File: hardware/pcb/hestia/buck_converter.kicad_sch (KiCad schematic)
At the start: 21 parts

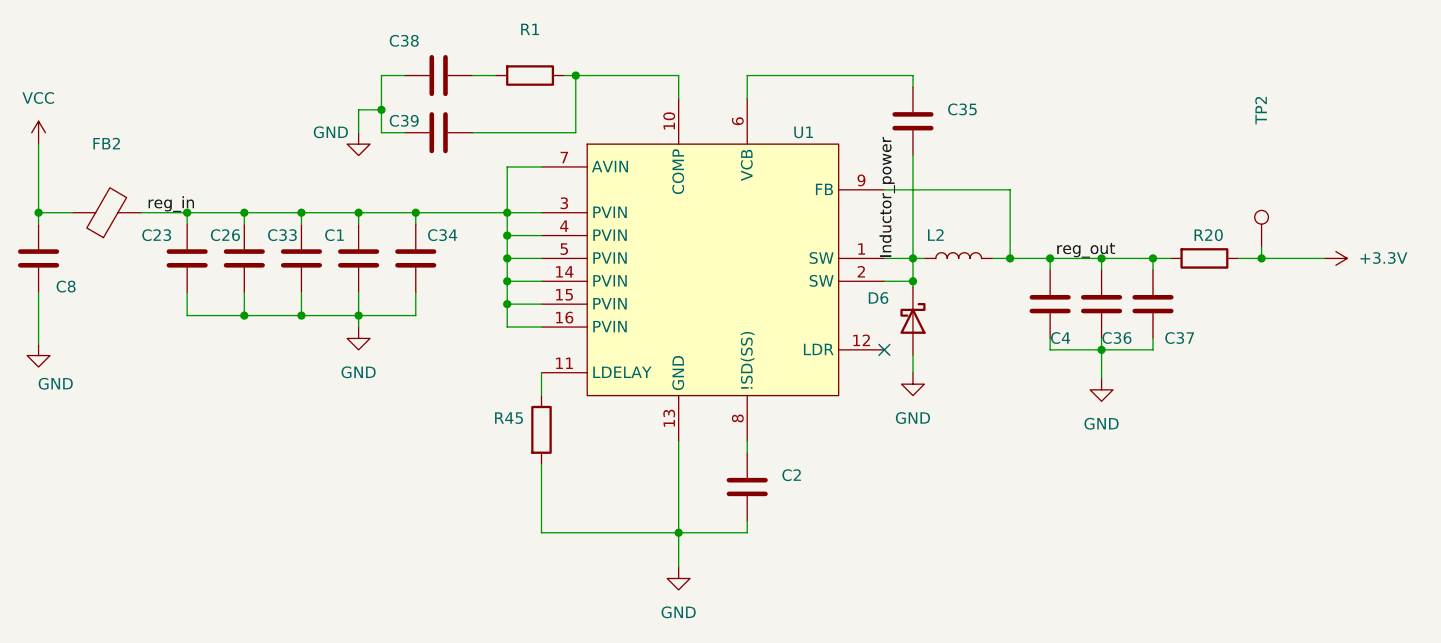
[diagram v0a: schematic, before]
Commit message: Fix some ERC violations
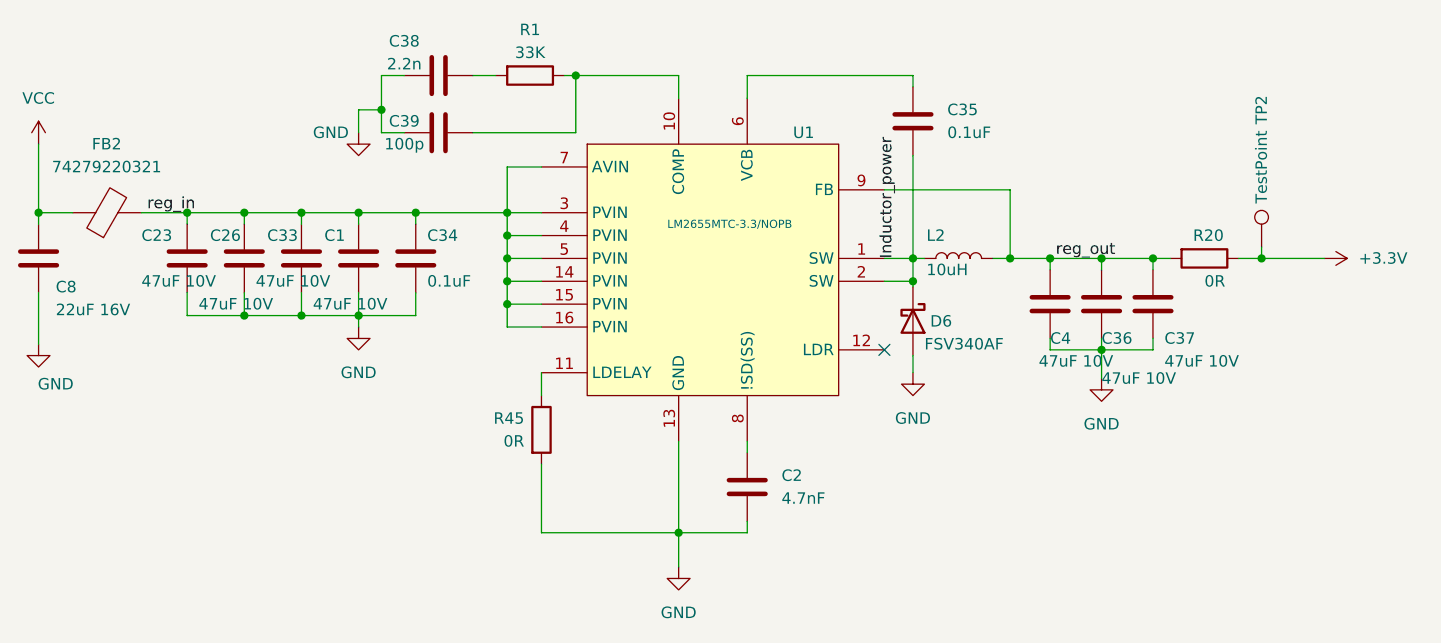
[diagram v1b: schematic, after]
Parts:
- C1, C23, C26, C33, C36, C37, C4: value (none) -> 47uF 10V; footprint (none) -> Capacitor_SMD:C_0805_2012Metric_Pad1.18x1.45mm_HandSolder
- C2: value (none) -> 4.7nF; footprint (none) -> Capacitor_SMD:C_0603_1608Metric_Pad1.08x0.95mm_HandSolder
- C34, C35: value (none) -> 0.1uF; footprint (none) -> Capacitor_SMD:C_0603_1608Metric_Pad1.08x0.95mm_HandSolder
- C38: value (none) -> 2.2n; footprint (none) -> Capacitor_SMD:C_0603_1608Metric_Pad1.08x0.95mm_HandSolder
- C39: value (none) -> 100p; footprint (none) -> Capacitor_SMD:C_0603_1608Metric_Pad1.08x0.95mm_HandSolder
- C8: value (none) -> 22uF 16V; footprint (none) -> Capacitor_SMD:C_1206_3216Metric
- D6: value (none) -> FSV340AF; footprint (none) -> Hestia:DO-214AD (SMAF)
- FB2: value (none) -> 74279220321; footprint (none) -> Resistor_SMD:R_0805_2012Metric_Pad1.20x1.40mm_HandSolder
- L2: value (none) -> 10uH; footprint (none) -> Inductor_SMD:L_Coilcraft_LPS5030
- R1: value (none) -> 33K; footprint (none) -> Resistor_SMD:R_0603_1608Metric_Pad0.98x0.95mm_HandSolder
- R20: value (none) -> 0R; footprint (none) -> Resistor_SMD:R_1210_3225Metric_Pad1.30x2.65mm_HandSolder
- R45: value (none) -> 0R; footprint (none) -> Resistor_SMD:R_0603_1608Metric_Pad0.98x0.95mm_HandSolder
- TP2: value (none) -> TestPoint; footprint (none) -> TestPoint:TestPoint_Pad_2.0x2.0mm
- U1: value (none) -> LM2655MTC-3.3/NOPB; footprint (none) -> Package_SO:TSSOP-16_4.4x5mm_P0.65mm
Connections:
- net +3V3 renamed +3.3V

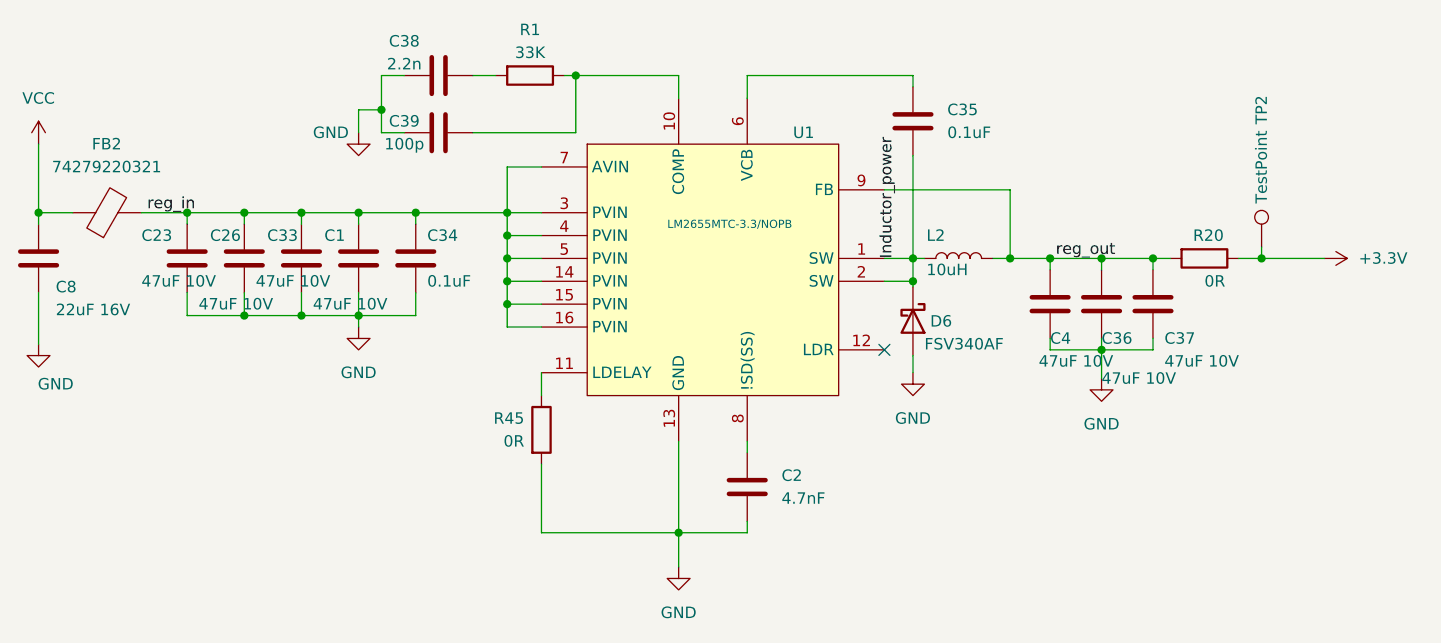
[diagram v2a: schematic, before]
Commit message: changed all 10K to 0.5% to be same component. changed led part numbers back to 0805. - my mistake. i had thought the footprints had changed to 0603. filled in other missing digikey part numbers. added manufacturer names and manufacturer part numbers. finished adding SMD/TH entry for component types. Excluded R4/R5 DNP part numbers from BOM
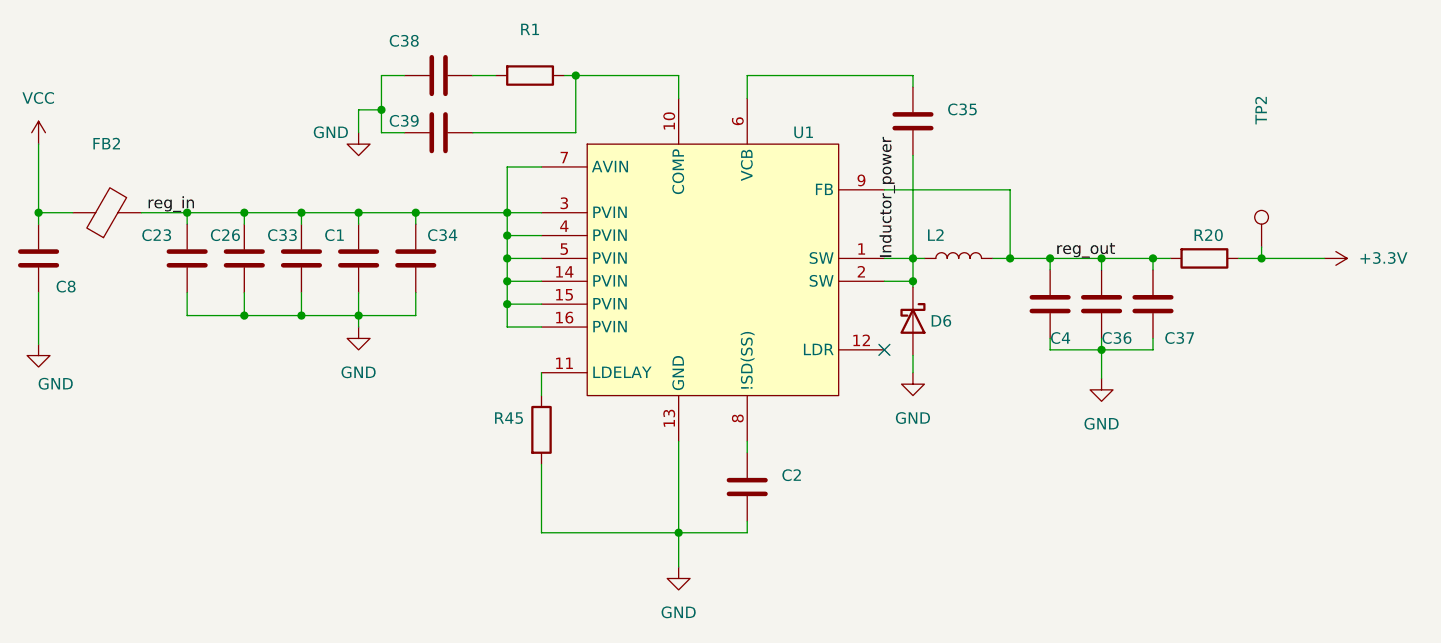
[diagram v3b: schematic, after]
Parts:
- C1, C23, C26, C33, C36, C37, C4: value 47uF 10V -> (none); footprint Capacitor_SMD:C_0805_2012Metric_Pad1.18x1.45mm_HandSolder -> (none); Manufacturer (none) -> Taiyo Yuden; Mfr PN (none) -> LMK212BBJ476MG-T
- C2: value 4.7nF -> (none); footprint Capacitor_SMD:C_0603_1608Metric_Pad1.08x0.95mm_HandSolder -> (none); Manufacturer (none) -> Samsung Electro-Mechanics; Mfr PN (none) -> CL10B472KB8WPNC
- C34, C35: value 0.1uF -> (none); footprint Capacitor_SMD:C_0603_1608Metric_Pad1.08x0.95mm_HandSolder -> (none); Manufacturer (none) -> Samsung Electro-Mechanics; Mfr PN (none) -> CL10B104KB8WPND
- C38: value 2.2n -> (none); footprint Capacitor_SMD:C_0603_1608Metric_Pad1.08x0.95mm_HandSolder -> (none); Manufacturer (none) -> KEMET; Mfr PN (none) -> C0603C222K5RACAUTO
- C39: value 100p -> (none); footprint Capacitor_SMD:C_0603_1608Metric_Pad1.08x0.95mm_HandSolder -> (none); Manufacturer (none) -> KYOCERA AVX; Mfr PN (none) -> 06035A100FAT2A
- C8: value 22uF 16V -> (none); footprint Capacitor_SMD:C_1206_3216Metric -> (none); Manufacturer (none) -> Samsung Electro-Mechanics; Mfr PN (none) -> CL31A226MOCLNNC; Type (none) -> SMD
- D6: value FSV340AF -> (none); footprint Hestia:DO-214AD (SMAF) -> (none); Manufacturer (none) -> onsemi; Mfr PN (none) -> FSV340AF
- FB2: value 74279220321 -> (none); footprint Resistor_SMD:R_0805_2012Metric_Pad1.20x1.40mm_HandSolder -> (none); Manufacturer (none) -> Würth Elektronik; Mfr PN (none) -> 74279220321
- L2: value 10uH -> (none); footprint Inductor_SMD:L_Coilcraft_LPS5030 -> (none); Manufacturer (none) -> Bourns Inc.; Mfr PN (none) -> SRP5030C-100M
- R1: value 33K -> (none); footprint Resistor_SMD:R_0603_1608Metric_Pad0.98x0.95mm_HandSolder -> (none); Digikey Part ERJ-PA3F3302V -> P33KBYCT-ND; Manufacturer (none) -> Panasonic Electronic Components; Mfr PN (none) -> ERJ-PA3F3302V
- R20: value 0R -> (none); footprint Resistor_SMD:R_1210_3225Metric_Pad1.30x2.65mm_HandSolder -> (none); Digikey Part (none) -> YAG3375CT-ND; Manufacturer (none) -> YAGEO; Mfr PN (none) -> RC1210JR-070RL
- R45: value 0R -> (none); footprint Resistor_SMD:R_0603_1608Metric_Pad0.98x0.95mm_HandSolder -> (none); Digikey Part (none) -> RMCF0603ZT0R00CT-ND; Manufacturer (none) -> Stackpole Electronics Inc; Mfr PN (none) -> RMCF0603ZT0R00
- TP2: value TestPoint -> (none); footprint TestPoint:TestPoint_Pad_2.0x2.0mm -> (none)
- U1: value LM2655MTC-3.3/NOPB -> (none); footprint Package_SO:TSSOP-16_4.4x5mm_P0.65mm -> (none); Manufacturer TI -> Texas Instruments; Mfr PN (none) -> LM2655MTC-3.3/NOPB

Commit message: c39 digikey and mfr part numbers changed to a 100pf part number. It had previously erroneously been given a 10pf part number
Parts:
- C39: Digikey Part 478-10285-1-ND -> 720-1649-1-ND; Manufacturer KYOCERA AVX -> Vishay Vitramon; Mfr PN 06035A100FAT2A -> VJ0603A101FXACW1BC
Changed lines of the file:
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@@
       (effects (font (size 1.27 1.27)) hide)
     )
-    (property "Digikey Part" "478-10285-1-ND" (id 5) (at 121.285 76.835 0)
+    (property "Digikey Part" "720-1649-1-ND" (id 5) (at 121.285 76.835 0)
       (effects (font (size 1.27 1.27)) hide)
     )
-    (property "Manufacturer" "KYOCERA AVX" (id 6) (at 121.285 76.835 0)
+    (property "Manufacturer" "Vishay Vitramon" (id 6) (at 121.285 76.835 0)
       (effects (font (size 1.27 1.27)) hide)
     )
-    (property "Mfr PN" "06035A100FAT2A" (id 7) (at 121.285 76.835 0)
+    (property "Mfr PN" "VJ0603A101FXACW1BC" (id 7) (at 121.285 76.835 0)
       (effects (font (size 1.27 1.27)) hide)
     )

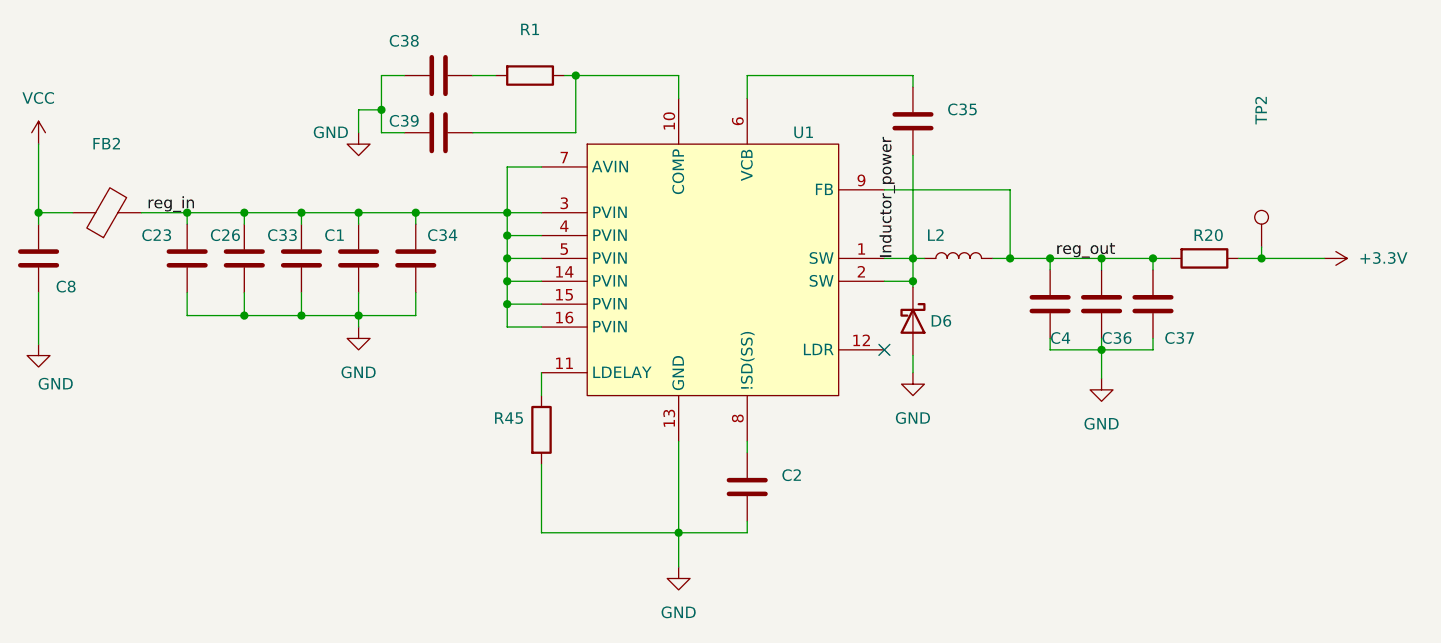
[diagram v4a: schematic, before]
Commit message: change d6? to SK34A-LTP with a DO-214AC (SMA) footprint. This diode is a higher profile and may violate height restrictions for some close stacked payload configurations.
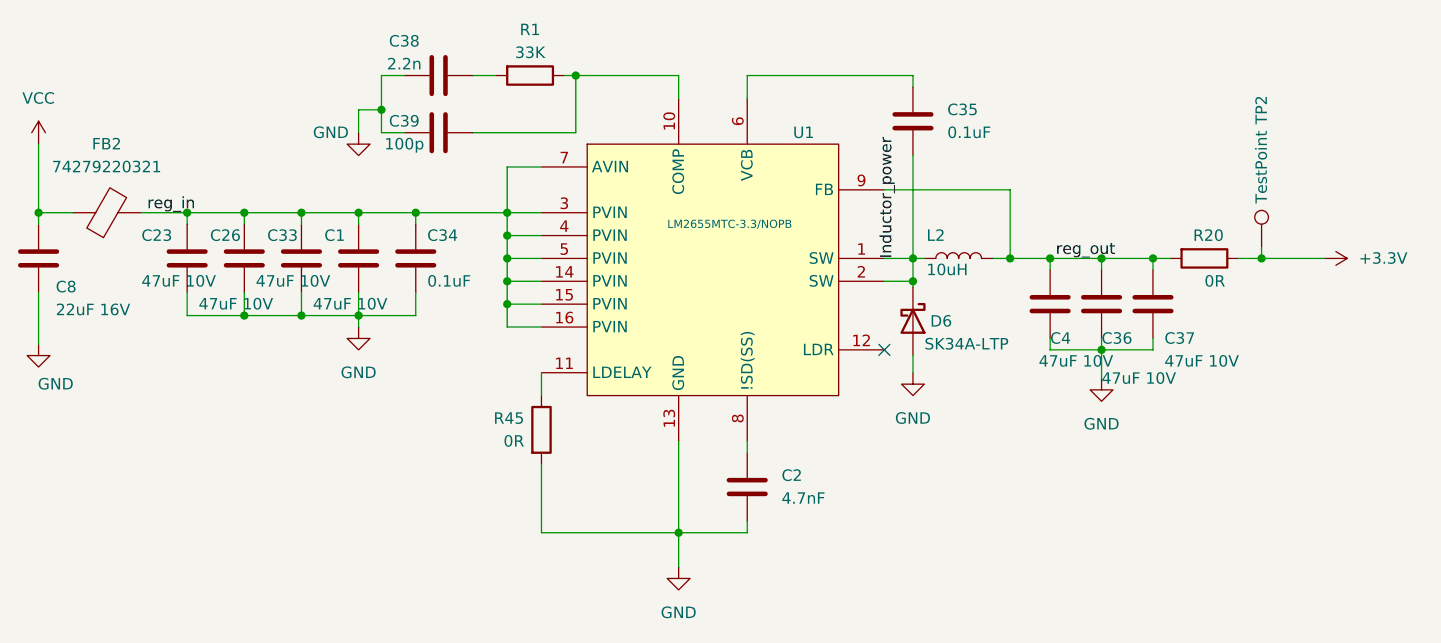
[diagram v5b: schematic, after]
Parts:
- C1, C23, C26, C33, C36, C37, C4: value (none) -> 47uF 10V; footprint (none) -> Capacitor_SMD:C_0805_2012Metric_Pad1.18x1.45mm_HandSolder
- C2: value (none) -> 4.7nF; footprint (none) -> Capacitor_SMD:C_0603_1608Metric_Pad1.08x0.95mm_HandSolder
- C34, C35: value (none) -> 0.1uF; footprint (none) -> Capacitor_SMD:C_0603_1608Metric_Pad1.08x0.95mm_HandSolder
- C38: value (none) -> 2.2n; footprint (none) -> Capacitor_SMD:C_0603_1608Metric_Pad1.08x0.95mm_HandSolder
- C39: value (none) -> 100p; footprint (none) -> Capacitor_SMD:C_0603_1608Metric_Pad1.08x0.95mm_HandSolder
- C8: value (none) -> 22uF 16V; footprint (none) -> Capacitor_SMD:C_1206_3216Metric
- D6: value (none) -> SK34A-LTP; footprint (none) -> Diode_SMD:D_SMA; Digikey Part FSV340AFCT-ND -> SK34A-LTPMSCT-ND; Manufacturer onsemi -> Micro Commercial Co; Mfr PN FSV340AF -> SK34A-LTP
- FB2: value (none) -> 74279220321; footprint (none) -> Resistor_SMD:R_0805_2012Metric_Pad1.20x1.40mm_HandSolder
- L2: value (none) -> 10uH; footprint (none) -> Inductor_SMD:L_Coilcraft_LPS5030
- R1: value (none) -> 33K; footprint (none) -> Resistor_SMD:R_0603_1608Metric_Pad0.98x0.95mm_HandSolder
- R20: value (none) -> 0R; footprint (none) -> Resistor_SMD:R_1210_3225Metric_Pad1.30x2.65mm_HandSolder
- R45: value (none) -> 0R; footprint (none) -> Resistor_SMD:R_0603_1608Metric_Pad0.98x0.95mm_HandSolder
- TP2: value (none) -> TestPoint; footprint (none) -> TestPoint:TestPoint_Pad_2.0x2.0mm
- U1: value (none) -> LM2655MTC-3.3/NOPB; footprint (none) -> Package_SO:TSSOP-16_4.4x5mm_P0.65mm
